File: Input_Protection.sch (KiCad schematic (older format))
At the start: 110 parts, among them U201 MOCD217M, U202 MOCD217M, U203 MOCD217M, U204 MOCD217M, U205 MOCD217M, U206 MOCD217M, U207 MOCD217M, U208 MOCD217M, U209 MOCD217M, U210 MOCD217M, U211 MOCD217M, U212 MOCD217M, U213 MOCD217M, U214 MOCD217M, U215 MOCD217M, U216 MOCD217M, U217 MOCD217M, U218 MOCD217M, U219 MOCD217M, U220 MOCD217M, U221 MOCD217M, U222 MOCD217M

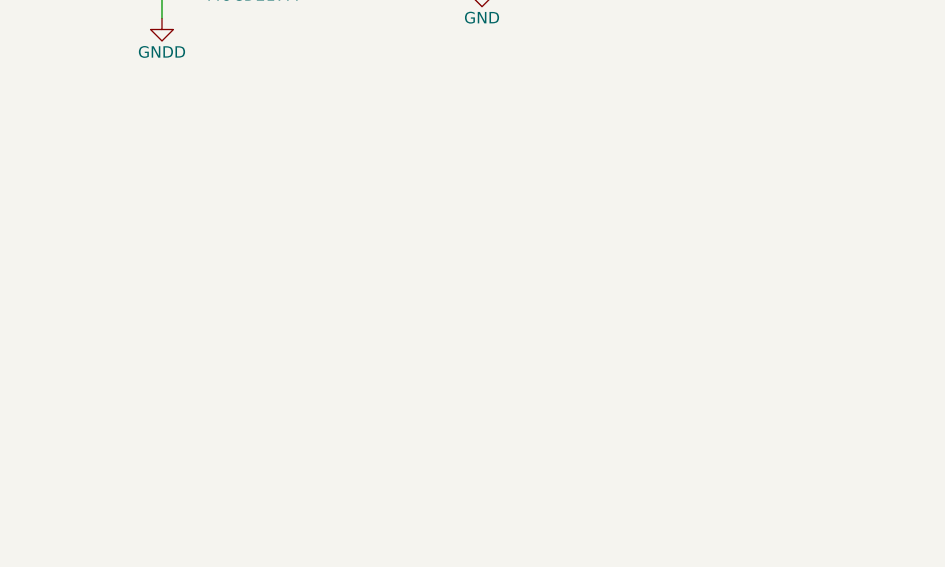
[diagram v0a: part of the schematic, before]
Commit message: footprints cleaned-up and submitted to oshpark!
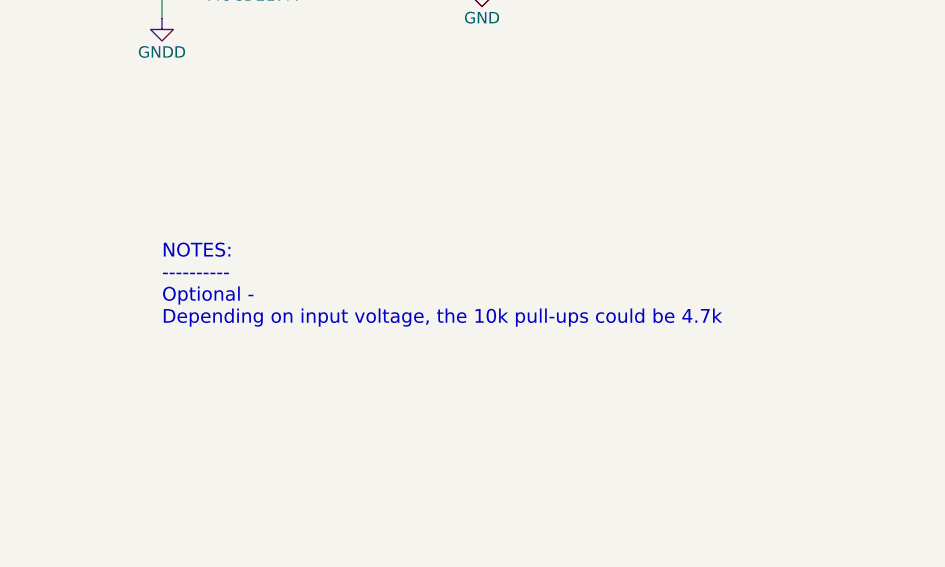
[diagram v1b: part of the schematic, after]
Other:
- note added: "NOTES:\n----------\nOptional -\nDepending on input voltage, the 10k pull-ups could be 4.7k"
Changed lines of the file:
@@
 	12950 3250 13650 3250
 Connection ~ 13650 3550
+Text Notes 12250 5150 0    60   ~ 0
+NOTES:\n----------\nOptional -\nDepending on input voltage, the 10k pull-ups could be 4.7k
 $EndSCHEMATC

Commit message: adding serial 1, 2, and 3 as protected inputs
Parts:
- added R289, R290, R291, R292, R293, R294: 10K, Resistors_SMD:R_0805, symbol R
- added R295, R296, R297, R298, R299, R300: 4.8k, Resistors_SMD:R_1206, symbol R
- added U223, U224, U225: MOCD217M, Housings_SOIC:SOIC-8_3.9x4.9mm_Pitch1.27mm, symbol MOCD213M
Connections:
- net +5V: now also R289.1, R290.1, R291.1, R292.1, R293.1, R294.1
- net GND: now also U223.2, U223.4, U224.2, U224.4, U225.2, U225.4
- net GNDD: now also U223.5, U223.7, U224.5, U224.7, U225.5, U225.7
- new net: R295.2, U223.1
- new net: R296.2, U223.3
- new net: R297.2, U224.1
- new net: R298.2, U224.3
- new net: R299.2, U225.1
- new net: R300.2, U225.3
- new net ARD_DIN14: R289.2, U223.6
- new net ARD_DIN15: R292.2, U223.8
- new net ARD_DIN16: R290.2, U224.6
- new net ARD_DIN17: R293.2, U224.8
- new net ARD_DIN18: R291.2, U225.6
- new net ARD_DIN19: R294.2, U225.8
- new net DIN14: R296.1
- new net DIN15: R295.1
- new net DIN16: R298.1
- new net DIN17: R297.1
- new net DIN18: R300.1
- new net DIN19: R299.1
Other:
- moved on the sheet: R201, R202, R203, R204, R205, R206, R207, R208, R209, R210, R211, R212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
